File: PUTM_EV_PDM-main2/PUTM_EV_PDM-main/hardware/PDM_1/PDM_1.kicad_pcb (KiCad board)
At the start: 2 copper layers, 60 x 90 mm, 43 parts, among them IC2 BTS722204ESAXUMA1, IC3 BTS722204ESAXUMA1, IC4 BTS722204ESAXUMA1, IC5 BTS722204ESAXUMA1, U1 STM32G0C1KCTxN, U2 LD1117S33TR_SOT223, U3 LM2675M-5, U5 MCP2542FDxMF

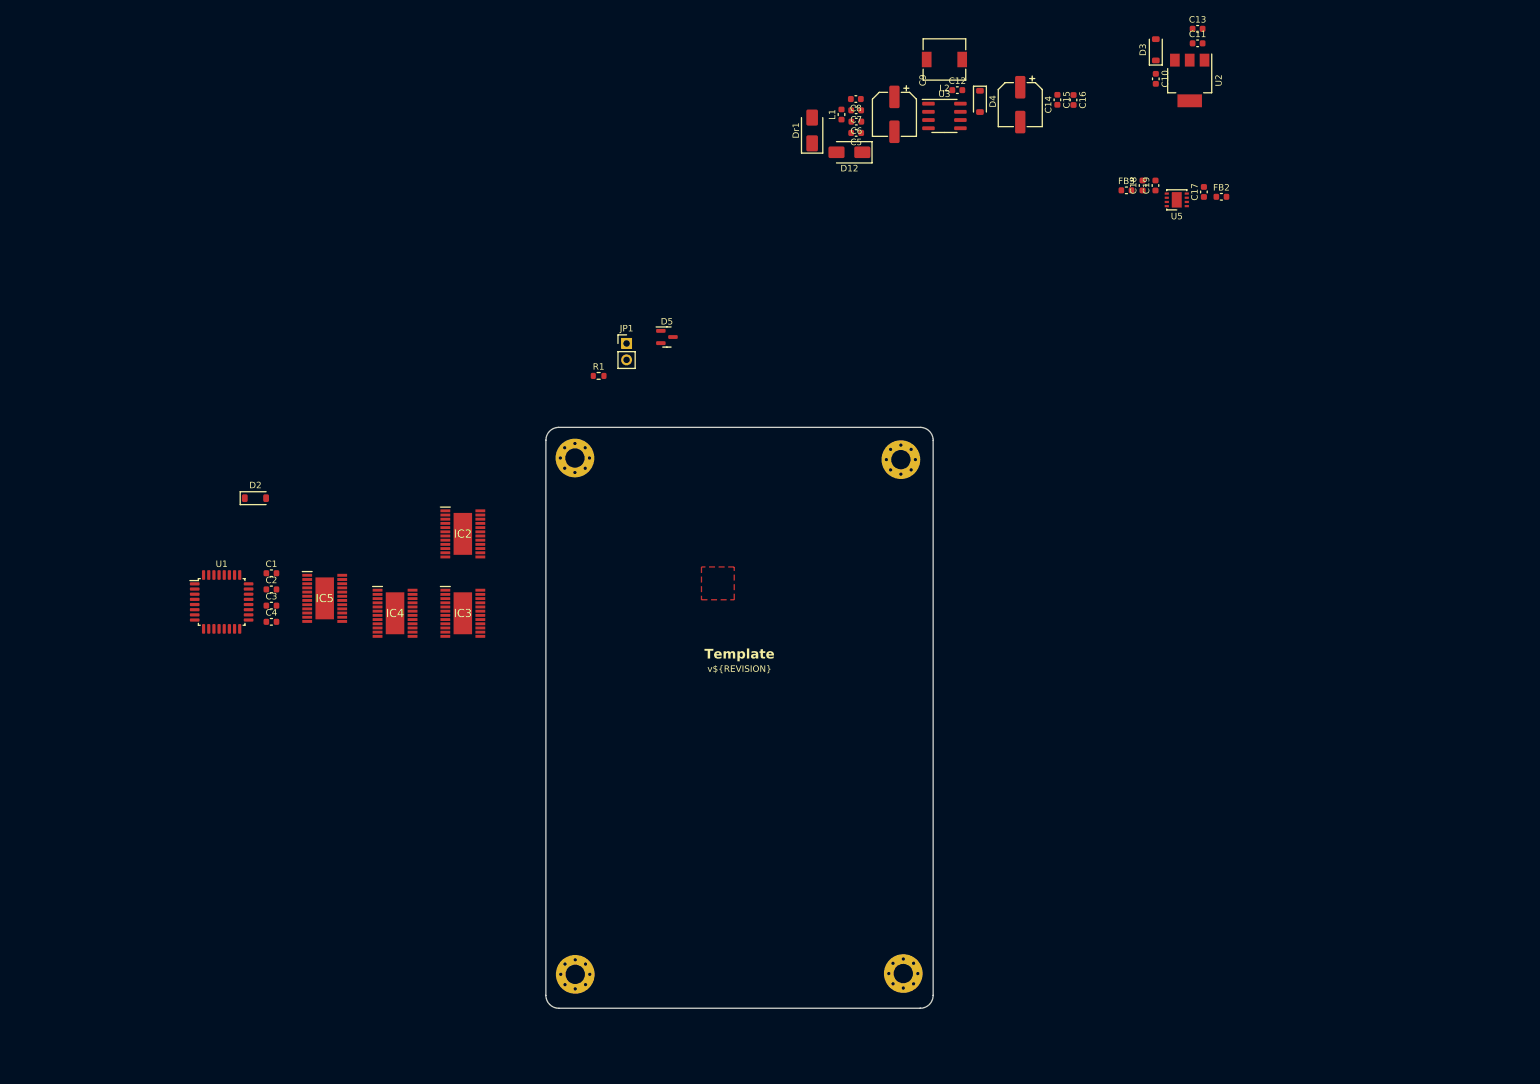
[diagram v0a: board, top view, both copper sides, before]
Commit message: lepsze footprinty
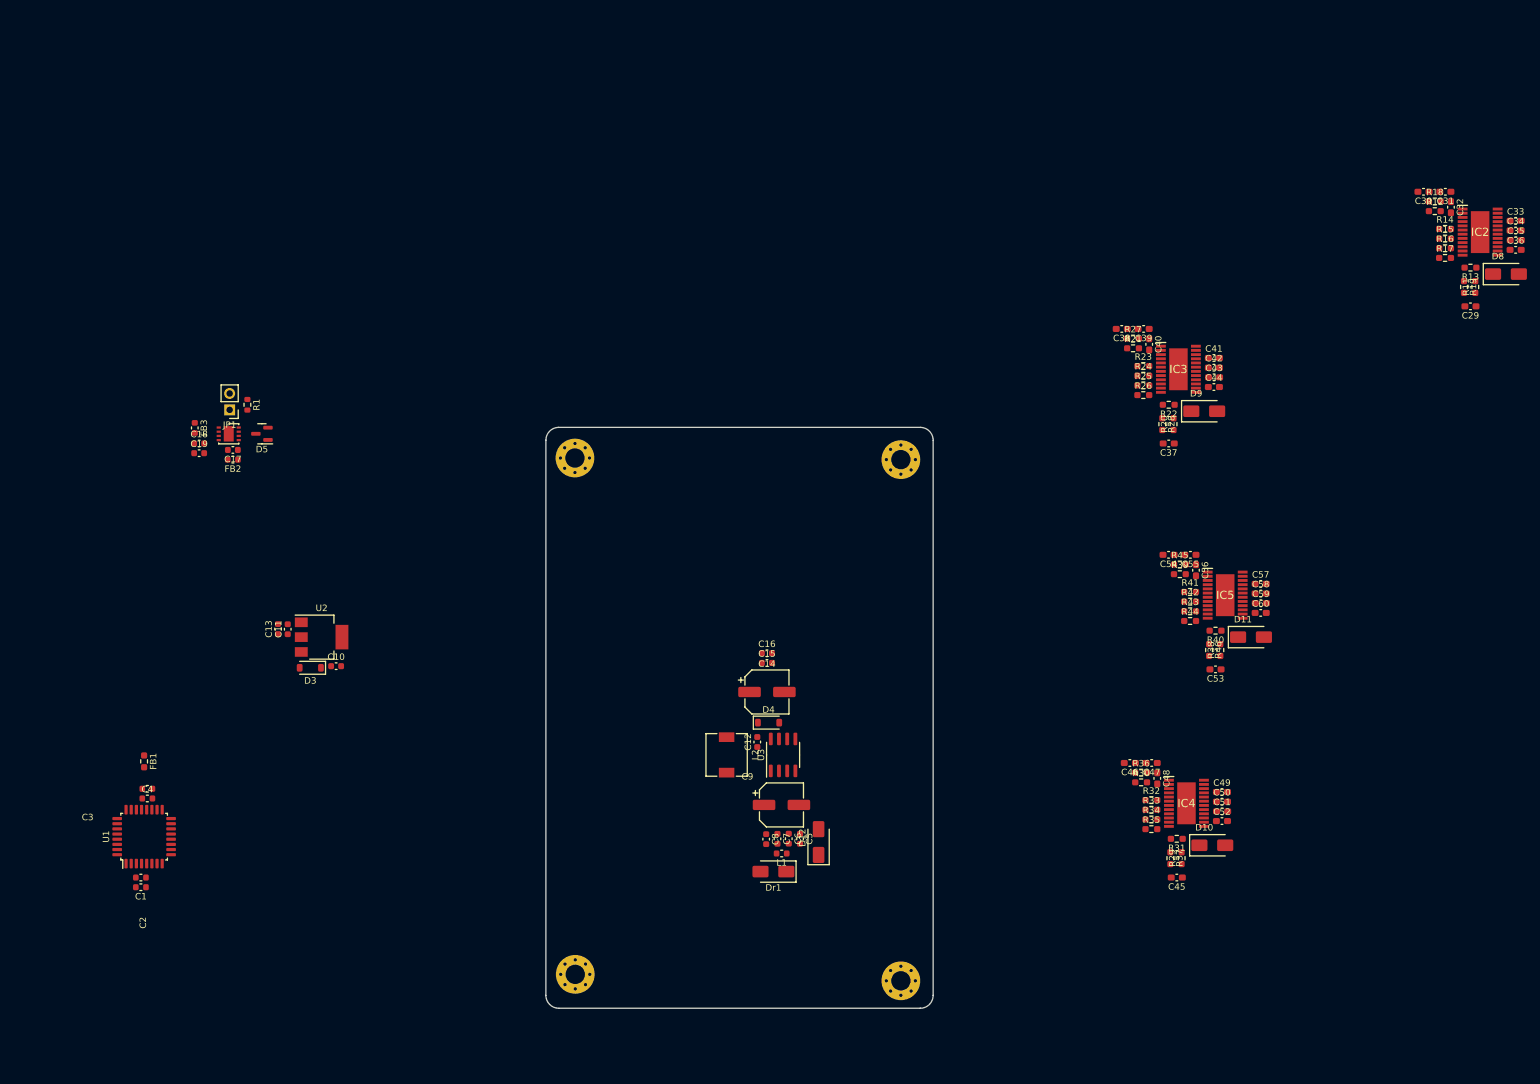
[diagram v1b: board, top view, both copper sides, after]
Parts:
- removed D2: D_Zener, Diode_SMD:D_SOD-123
- added C29: 220p, Capacitor_SMD:C_0603_1608Metric_Pad1.08x0.95mm_HandSolder, F.Cu at (259.2, 57.2)
- added C30: 100n, Capacitor_SMD:C_0603_1608Metric_Pad1.08x0.95mm_HandSolder, F.Cu at (252.0, 39.5)
- added C31: 22n, Capacitor_SMD:C_0603_1608Metric_Pad1.08x0.95mm_HandSolder, F.Cu at (255.4, 39.5)
- added C32: 470n, Capacitor_SMD:C_0603_1608Metric_Pad1.08x0.95mm_HandSolder, F.Cu at (256.2, 41.9)
- added C33: 10n, Capacitor_SMD:C_0603_1608Metric_Pad1.08x0.95mm_HandSolder, F.Cu at (266.2, 44.0)
- added C34: 10n, Capacitor_SMD:C_0603_1608Metric_Pad1.08x0.95mm_HandSolder, F.Cu at (266.2, 45.5)
- added C35: 10n, Capacitor_SMD:C_0603_1608Metric_Pad1.08x0.95mm_HandSolder, F.Cu at (266.3, 47.0)
- added C36: 10n, Capacitor_SMD:C_0603_1608Metric_Pad1.08x0.95mm_HandSolder, F.Cu at (266.2, 48.5)
- added C37: 220p, Capacitor_SMD:C_0603_1608Metric_Pad1.08x0.95mm_HandSolder, F.Cu at (212.5, 78.5)
- added C38: 100n, Capacitor_SMD:C_0603_1608Metric_Pad1.08x0.95mm_HandSolder, F.Cu at (205.2, 60.8)
- added C39: 22n, Capacitor_SMD:C_0603_1608Metric_Pad1.08x0.95mm_HandSolder, F.Cu at (208.6, 60.8)
- added C40: 470n, Capacitor_SMD:C_0603_1608Metric_Pad1.08x0.95mm_HandSolder, F.Cu at (209.5, 63.1)
- added C41: 10n, Capacitor_SMD:C_0603_1608Metric_Pad1.08x0.95mm_HandSolder, F.Cu at (219.5, 65.2)
- added C42: 10n, Capacitor_SMD:C_0603_1608Metric_Pad1.08x0.95mm_HandSolder, F.Cu at (219.5, 66.8)
- added C43: 10n, Capacitor_SMD:C_0603_1608Metric_Pad1.08x0.95mm_HandSolder, F.Cu at (219.5, 68.2)
- added C44: 10n, Capacitor_SMD:C_0603_1608Metric_Pad1.08x0.95mm_HandSolder, F.Cu at (219.5, 69.8)
- added C45: 220p, Capacitor_SMD:C_0603_1608Metric_Pad1.08x0.95mm_HandSolder, F.Cu at (213.8, 145.8)
- added C46: 100n, Capacitor_SMD:C_0603_1608Metric_Pad1.08x0.95mm_HandSolder, F.Cu at (206.5, 128.0)
- added C47: 22n, Capacitor_SMD:C_0603_1608Metric_Pad1.08x0.95mm_HandSolder, F.Cu at (209.9, 128.0)
- added C48: 470n, Capacitor_SMD:C_0603_1608Metric_Pad1.08x0.95mm_HandSolder, F.Cu at (210.7, 130.4)
- added C49: 10n, Capacitor_SMD:C_0603_1608Metric_Pad1.08x0.95mm_HandSolder, F.Cu at (220.8, 132.5)
- added C50: 10n, Capacitor_SMD:C_0603_1608Metric_Pad1.08x0.95mm_HandSolder, F.Cu at (220.8, 134.0)
- added C51: 10n, Capacitor_SMD:C_0603_1608Metric_Pad1.08x0.95mm_HandSolder, F.Cu at (220.8, 135.5)
- added C52: 10n, Capacitor_SMD:C_0603_1608Metric_Pad1.08x0.95mm_HandSolder, F.Cu at (220.8, 137.0)
- added C53: 220p, Capacitor_SMD:C_0603_1608Metric_Pad1.08x0.95mm_HandSolder, F.Cu at (219.8, 113.5)
- added C54: 100n, Capacitor_SMD:C_0603_1608Metric_Pad1.08x0.95mm_HandSolder, F.Cu at (212.5, 95.8)
- added C55: 22n, Capacitor_SMD:C_0603_1608Metric_Pad1.08x0.95mm_HandSolder, F.Cu at (215.9, 95.8)
- added C56: 470n, Capacitor_SMD:C_0603_1608Metric_Pad1.08x0.95mm_HandSolder, F.Cu at (216.7, 98.1)
- added C57: 10n, Capacitor_SMD:C_0603_1608Metric_Pad1.08x0.95mm_HandSolder, F.Cu at (226.8, 100.2)
- added C58: 10n, Capacitor_SMD:C_0603_1608Metric_Pad1.08x0.95mm_HandSolder, F.Cu at (226.8, 101.8)
- added C59: 10n, Capacitor_SMD:C_0603_1608Metric_Pad1.08x0.95mm_HandSolder, F.Cu at (226.8, 103.2)
- added C60: 10n, Capacitor_SMD:C_0603_1608Metric_Pad1.08x0.95mm_HandSolder, F.Cu at (226.8, 104.8)
- added D10: D_Schottky, Diode_SMD:D_SMA, F.Cu at (219.2, 140.8)
- added D11: D_Schottky, Diode_SMD:D_SMA, F.Cu at (225.2, 108.5)
- added D8: D_Schottky, Diode_SMD:D_SMA, F.Cu at (264.8, 52.2)
- added D9: D_Schottky, Diode_SMD:D_SMA, F.Cu at (218.0, 73.5)
- added FB1: FerriteBead_Small, Resistor_SMD:R_0603_1608Metric_Pad0.98x0.95mm_HandSolder, F.Cu at (53.8, 127.8)
- added R11: 4.7k, Resistor_SMD:R_0603_1608Metric_Pad0.98x0.95mm_HandSolder, F.Cu at (260.0, 54.2)
- added R12: 470, Resistor_SMD:R_0603_1608Metric_Pad0.98x0.95mm_HandSolder, F.Cu at (253.7, 42.5)
- added R13: 4.7k, Resistor_SMD:R_0603_1608Metric_Pad0.98x0.95mm_HandSolder, F.Cu at (259.2, 51.2)
- added R14: 4.7k, Resistor_SMD:R_0603_1608Metric_Pad0.98x0.95mm_HandSolder, F.Cu at (255.3, 45.2)
- added R15: 4.7k, Resistor_SMD:R_0603_1608Metric_Pad0.98x0.95mm_HandSolder, F.Cu at (255.3, 46.8)
- added R16: 4.7k, Resistor_SMD:R_0603_1608Metric_Pad0.98x0.95mm_HandSolder, F.Cu at (255.3, 48.2)
- added R17: 4.7k, Resistor_SMD:R_0603_1608Metric_Pad0.98x0.95mm_HandSolder, F.Cu at (255.3, 49.8)
- added R18: 47, Resistor_SMD:R_0603_1608Metric_Pad0.98x0.95mm_HandSolder, F.Cu at (253.7, 41.0)
- added R19: 1.2k, Resistor_SMD:R_0603_1608Metric_Pad0.98x0.95mm_HandSolder, F.Cu at (258.2, 54.2)
- added R20: 4.7k, Resistor_SMD:R_0603_1608Metric_Pad0.98x0.95mm_HandSolder, F.Cu at (213.2, 75.5)
- added R21: 470, Resistor_SMD:R_0603_1608Metric_Pad0.98x0.95mm_HandSolder, F.Cu at (207.0, 63.8)
- added R22: 4.7k, Resistor_SMD:R_0603_1608Metric_Pad0.98x0.95mm_HandSolder, F.Cu at (212.5, 72.5)
- added R23: 4.7k, Resistor_SMD:R_0603_1608Metric_Pad0.98x0.95mm_HandSolder, F.Cu at (208.6, 66.5)
- added R24: 4.7k, Resistor_SMD:R_0603_1608Metric_Pad0.98x0.95mm_HandSolder, F.Cu at (208.6, 68.0)
- added R25: 4.7k, Resistor_SMD:R_0603_1608Metric_Pad0.98x0.95mm_HandSolder, F.Cu at (208.6, 69.5)
- added R26: 4.7k, Resistor_SMD:R_0603_1608Metric_Pad0.98x0.95mm_HandSolder, F.Cu at (208.6, 71.0)
- added R27: 47, Resistor_SMD:R_0603_1608Metric_Pad0.98x0.95mm_HandSolder, F.Cu at (207.0, 62.2)
- added R28: 1.2k, Resistor_SMD:R_0603_1608Metric_Pad0.98x0.95mm_HandSolder, F.Cu at (211.5, 75.5)
- added R29: 4.7k, Resistor_SMD:R_0603_1608Metric_Pad0.98x0.95mm_HandSolder, F.Cu at (214.5, 142.8)
- added R30: 470, Resistor_SMD:R_0603_1608Metric_Pad0.98x0.95mm_HandSolder, F.Cu at (208.2, 131.0)
- added R31: 4.7k, Resistor_SMD:R_0603_1608Metric_Pad0.98x0.95mm_HandSolder, F.Cu at (213.8, 139.8)
- added R32: 4.7k, Resistor_SMD:R_0603_1608Metric_Pad0.98x0.95mm_HandSolder, F.Cu at (209.8, 133.8)
- added R33: 4.7k, Resistor_SMD:R_0603_1608Metric_Pad0.98x0.95mm_HandSolder, F.Cu at (209.8, 135.2)
- added R34: 4.7k, Resistor_SMD:R_0603_1608Metric_Pad0.98x0.95mm_HandSolder, F.Cu at (209.8, 136.8)
- added R35: 4.7k, Resistor_SMD:R_0603_1608Metric_Pad0.98x0.95mm_HandSolder, F.Cu at (209.8, 138.2)
- added R36: 47, Resistor_SMD:R_0603_1608Metric_Pad0.98x0.95mm_HandSolder, F.Cu at (208.2, 129.5)
- added R37: 1.2k, Resistor_SMD:R_0603_1608Metric_Pad0.98x0.95mm_HandSolder, F.Cu at (212.8, 142.8)
- added R38: 4.7k, Resistor_SMD:R_0603_1608Metric_Pad0.98x0.95mm_HandSolder, F.Cu at (220.5, 110.5)
- added R39: 470, Resistor_SMD:R_0603_1608Metric_Pad0.98x0.95mm_HandSolder, F.Cu at (214.2, 98.8)
- added R40: 4.7k, Resistor_SMD:R_0603_1608Metric_Pad0.98x0.95mm_HandSolder, F.Cu at (219.8, 107.5)
- added R41: 4.7k, Resistor_SMD:R_0603_1608Metric_Pad0.98x0.95mm_HandSolder, F.Cu at (215.8, 101.5)
- added R42: 4.7k, Resistor_SMD:R_0603_1608Metric_Pad0.98x0.95mm_HandSolder, F.Cu at (215.8, 103.0)
- added R43: 4.7k, Resistor_SMD:R_0603_1608Metric_Pad0.98x0.95mm_HandSolder, F.Cu at (215.8, 104.5)
- added R44: 4.7k, Resistor_SMD:R_0603_1608Metric_Pad0.98x0.95mm_HandSolder, F.Cu at (215.8, 106.0)
- added R45: 47, Resistor_SMD:R_0603_1608Metric_Pad0.98x0.95mm_HandSolder, F.Cu at (214.2, 97.2)
- added R46: 1.2k, Resistor_SMD:R_0603_1608Metric_Pad0.98x0.95mm_HandSolder, F.Cu at (218.8, 110.5)
- D12: value D_TVS -> PESD24VF1BLYL
- moved C13 170.1 mm to (74.5, 107.2), turned to 90 degrees
- moved C11 167.7 mm to (76.0, 107.3), turned to 90 degrees
- moved IC2 164.4 mm to (260.8, 45.8)
- moved D3 162.3 mm to (79.5, 113.2), turned to 180 degrees
- moved U2 159.8 mm to (81.2, 108.5), turned to 0 degrees
- moved FB2 158.5 mm to (67.5, 81.0), turned to 180 degrees
- moved C10 156.2 mm to (83.5, 113.0), turned to 0 degrees
- moved C17 155.7 mm to (67.5, 79.5), turned to 180 degrees
- moved C19 153.9 mm to (62.3, 80.0), turned to 0 degrees
- moved C18 151.5 mm to (62.3, 78.5), turned to 0 degrees
- moved U5 151.3 mm to (66.9, 77.0), turned to 0 degrees
- moved FB3 149.0 mm to (61.6, 76.1), turned to -90 degrees
- moved IC5 139.5 mm to (221.2, 102.0)
- moved IC4 126.1 mm to (215.2, 134.2)
- moved IC3 117.1 mm to (214.0, 67.0)
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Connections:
- D12 pad 1: GND -> /power/VIN_L
- D12 pad 2: /power/VIN_L -> GND
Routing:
- removed copper zone on F.Cu, net /power/VIN_SW_REG
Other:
- copper layers 2 -> 4
- board text removed: "Template"
- board text removed: "v${REVISION}"
